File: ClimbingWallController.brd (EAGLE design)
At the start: 100 x 80 mm, 336 parts, among them IC1 74HCT138D, IC2 74HCT138D, IC3 PIC24FJ32GB004, IC4 SN74LV4052AD, IC5 SN74LV4052AD, IC6 TC1015, IC7 NCP1117, J1 PWR, Q1 NC, Q10 DPBT8105, Q11 DPBT8105, Q12 DPBT8105, Q13 DPBT8105, Q14 DPBT8105, Q15 DPBT8105, Q16 DPBT8105, Q18 DPBT8105, Q2 DPBT8105, Q3 DPBT8105, Q4 DPBT8105, Q5 DPBT8105, Q6 DPBT8105, Q7 DPBT8105, Q8 DPBT8105, Q9 DPBT8105, X1 MINI-USB-32005-201

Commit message: Iterated through a few possible board floorplans.  Routing will be incredibly tight, but I thought of a few possibilities that ease those concerns.
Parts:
- removed Q18: DPBT8105, Parts:SOT23
- removed ROW0: (no value), Parts:OSTVN08
- removed SG1: NC, buzzer:F/CM04P
- added JP2: BUZZER, pinhead:1X02
- added Q17: NC, transistor:SOT23-EBC
- added ROW2: (no value), Parts:OSTVN08
- C1, C9: value 10uF -> 22n; device rcl:C1206K -> resistor:C0603
- C10, C15: value 1uF -> 22n; device rcl:C0805 -> resistor:C0603
- C11, C12, C13, C14, C3, C4, C5: value 0.1uF -> 22n; device rcl:C0805 -> resistor:C0603
- C16: value 0.1uF -> NC; device rcl:C0805 -> rcl:C0603K
- C17, C29: value 1uF -> 0.1uF; device rcl:C0805 -> rcl:C0603K
- C18, C39, C89, C90, C91, C92, C93, C94, C95, C96, C97, C98: device rcl:C0805 -> rcl:C0603K
- C19: value 100uF -> 0.1uF; device resistor:PANASONIC_D -> rcl:C0603K
- C2, C6, C7: value NC -> 22n; device rcl:C0805 -> resistor:C0603
- C20: device resistor:C0805 -> resistor:C0603
- C21: value 100uF -> NC; device resistor:PANASONIC_D -> rcl:C0603K
- C22: value 22n -> NC; device resistor:C0805 -> rcl:C0603K
- C23: value 22n -> 470pF; device resistor:C0805 -> rcl:C0805
- C24, C38: value 22n -> 10uF; device resistor:C0805 -> rcl:C1206K
- C25: value 22n -> 1uF; device resistor:C0805 -> rcl:C0805
- C26, C27, C28, C31, C33: value 22n -> 0.1uF; device resistor:C0805 -> rcl:C0603K
- C30: value 100uF -> 1uF; device resistor:PANASONIC_D -> rcl:C0603K
- C32, C36: value 22n -> 1uF; device resistor:C0805 -> rcl:C0603K
- C34, C35, C37: value 22n -> 100uF; device resistor:C0805 -> resistor:PANASONIC_D
- C41, C42, C43, C44, C45, C46, C47, C48, C49, C50, C51, C52, C53, C54, C55, C56, C57, C58, C59, C60, C61, C62, C63, C64, C65, C66, C67, C68, C69, C70, C71, C72, C73, C74, C75, C76, C77, C78, C79, C80, C81, C82, C83, C84, C85, C86, C87, C88: device resistor:C0805 -> resistor:C0603K
- C8: value 470pF -> 22n; device rcl:C0805 -> resistor:C0603
- Q1: value NC -> DPBT8105; device transistor:SOT23-EBC -> Parts:SOT23
- R1, R10, R4: value 4.7k -> 20; device resistor:R0805 -> resistor:R0603
- R100, R101, R102, R103, R104, R105, R106, R107, R108, R109, R110, R111, R112, R113, R114, R115, R116, R117, R118, R119, R120, R121, R122, R123, R124, R125, R126, R127, R128, R129, R130, R131, R132, R133, R134, R135, R39, R40, R41, R42, R43, R44, R45, R46, R47, R48, R87, R88, R89, R90, R91, R92, R93, R94, R95, R96, R97, R98, R99: device resistor:R0805 -> resistor:R0603
- R11, R2, R5: value 4.7k -> 750; device resistor:R0805 -> resistor:R0603
- R12, R3, R6, R9: value 4.7k -> NC; device resistor:R0805 -> resistor:R0603
- R13, R16, R19, R22, R25, R28, R31, R34: value 390 -> 20; device resistor:R0805 -> resistor:R0603
- R14, R17, R20, R23, R26, R29, R32, R35: value 390 -> 750; device resistor:R0805 -> resistor:R0603
- R15, R18, R21, R24, R27, R30, R33: value 390 -> NC; device resistor:R0805 -> resistor:R0603
- R36: value 0 -> NC; device resistor:R0805 -> resistor:R0603
- R37: value NC -> 20; device resistor:R0805 -> resistor:R0603
- R38: value NC -> 750; device resistor:R0805 -> resistor:R0603
- R49, R52, R58: value 20 -> 4.7k; device resistor:R0805 -> resistor:R0603
- R50, R53, R59: value 750 -> 4.7k; device resistor:R0805 -> resistor:R0603
- R51, R54, R57, R60: value NC -> 4.7k; device resistor:R0805 -> resistor:R0603
- R55: value 20 -> 1.37k 0.5%
- R56: value 750 -> 1.37k 0.5%
- R61, R64, R67, R70, R73, R76, R79, R82: value 20 -> 390; device resistor:R0805 -> resistor:R0603
- R62, R65, R68, R71, R74, R77, R80, R83: value 750 -> 390; device resistor:R0805 -> resistor:R0603
- R63, R66, R69, R72, R75, R78, R81: value NC -> 390; device resistor:R0805 -> resistor:R0603
- R7: value 1.37k 0.5% -> 20; device resistor:R0805 -> resistor:R0603
- R8: value 1.37k 0.5% -> 750; device resistor:R0805 -> resistor:R0603
- R84: value NC -> 0
- R85: value 20 -> NC; device resistor:R0805 -> resistor:R0603
- R86: value 750 -> NC; device resistor:R0805 -> resistor:R0603
- moved C90 277.2 mm to (92.7, -58.4)
- moved C24 273.5 mm to (44.5, -102.9)
- moved C23 271.1 mm to (96.5, -49.5)
- moved C89 268.3 mm to (87.6, -58.4)
- moved D20 265.0 mm to (91.4, 26.7)
- moved C17 264.1 mm to (102.9, -49.5)
- moved C39 259.4 mm to (82.5, -58.4)
- moved C25 257.6 mm to (62.2, -58.4)
- moved D30 257.5 mm to (91.4, 52.1)
- moved C1 255.2 mm to (76.5, 11.7), turned to 270 degrees
- moved D19 253.4 mm to (91.4, 24.1)
- moved D40 251.4 mm to (91.4, 77.5)
- moved C18 250.7 mm to (109.2, -49.5)
- moved C61 246.6 mm to (88.6, 69.8)
- moved D29 245.3 mm to (91.4, 49.5)
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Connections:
- removed net N$31: Q1.B, R39.2
- removed net N$32: Q1.C, SG1.-
- removed net N$35: Q3.1, R44.2, R45.2
- removed net N$36: C22.1, R43.1
- removed net N$37: Q4.1, R47.2, R48.2
- removed net N$38: C23.1, R46.1
- removed net N$39: Q5.1, R50.2, R51.2
- removed net N$40: C24.1, R49.1
- removed net N$49: Q18.1, R65.2, R66.2
- removed net N$50: C31.1, R64.1
- removed net N$51: Q10.1, R68.2, R69.2
- removed net N$52: C32.1, R67.1
- removed net N$53: Q11.1, R71.2, R72.2
- removed net N$54: C33.1, R70.1
- removed net N$55: Q12.1, R74.2, R75.2
- removed net N$56: C34.1, R73.1
- removed net N$57: Q13.1, R77.2, R78.2
- removed net N$58: C35.1, R76.1
- removed net N$59: Q14.1, R80.2, R81.2
- removed net N$60: C36.1, R79.1
- removed net N$61: Q15.1, R83.2, R84.2
- removed net N$62: C37.1, R82.1
- removed net N$63: Q16.1, R86.2, R87.2
- removed net N$64: C38.1, R85.1
- new net N$65: R64.2, TCH0.3
- new net N$66: R65.2, TCH0.4
- new net N$67: R66.2, TCH0.5
- new net N$68: R67.2, TCH0.6
- new net N$69: R68.2, TCH0.7
- new net N$70: R69.2, TCH0.8
- new net N$71: R70.2, TCH0.9
- new net N$72: R71.2, TCH0.10
- new net N$73: R72.2, TCH0.11
- new net N$74: R74.2, TCH1.2
- new net N$75: R76.2, TCH1.4
- new net N$76: R78.2, TCH1.6
- new net N$77: R80.2, TCH1.8
- new net N$78: R82.2, TCH1.10
- new net N$79: R73.2, TCH1.1
- new net N$80: R75.2, TCH1.3
- new net N$81: R77.2, TCH1.5
- new net N$82: R79.2, TCH1.7
- new net N$83: R81.2, TCH1.9
- new net N$84: R83.2, TCH1.11
- new net N$85: C23.1, IC6.4
- new net N$86: R85.1, R86.2
- new net N$87: Q17.B, R87.2
- new net N$88: JP2.2, Q17.C
- net +3V3: now also C19.1, C24.1, C26.1, C27.1, C30.1, C31.1, C32.1, C33.1, R60.2, R85.2; no longer C11.1, C12.1, C15.1, C16.1, C3.1, C4.1, C5.1, C9.1, R12.2, R37.2
- net +5V: now also C25.1, C28.1, C34.+, C36.1, C37.+, JP2.1, Q1.2, R12.1, R15.1, R18.1, R21.1, R24.1, R27.1, R3.1, R30.1, R33.1, R36.1, R39.1, R6.1, R84.2, R9.1; no longer C10.1, C13.1, C14.1, C21.+, C30.+, Q18.2, R36.2, R51.1, R54.1, R57.1, R60.1, R63.1, R66.1, R69.1, R72.1, R75.1, R78.1, R81.1, R84.1, R87.1, SG1.+
- net CAIREF: now also R55.2; no longer R7.2
- net CAIREF1: now also R56.2; no longer R8.2
- net DISVREG: now also R59.2; no longer R11.2
- net GND: now also C19.2, C21.2, C30.2, C34.-, C35.-, C37.-, Q17.E, R49.1, R50.1, R51.1, R52.1, R53.1, R54.1, R55.1, R56.1, R57.1, R59.1, R86.1; no longer C19.-, C21.-, C30.-, C34.2, C35.2, C37.2, Q1.E, R1.1, R11.1, R2.1, R3.1, R38.1, R4.1, R5.1, R6.1, R7.1, R8.1, R9.1
- net MCLR_: now also R61.1; no longer R13.1
- net N$1: now also Q1.1, R2.2, R3.2; no longer C2.1, R12.1, R13.2
- net N$10: now also C5.1, R13.1; no longer R17.2, TCH0.4
- net N$11: now also Q7.1, R17.2; no longer TCH0.5
- net N$12: now also C6.1, R16.1; no longer R19.2, TCH0.6
- net N$13: now also Q8.1, R21.2; no longer TCH0.7
- net N$14: now also C7.1, R19.1; no longer R21.2, TCH0.8
- net N$15: now also Q9.1, R23.2, R24.2; no longer R22.2, TCH0.9
- net N$16: now also C8.1, R22.1; no longer R23.2, TCH0.10
- net N$17: now also Q10.1, R26.2, R27.2; no longer R24.2, TCH0.11
- net N$18: now also C9.1, R25.1; no longer R26.2, TCH1.2
- net N$19: now also Q11.1, R29.2, R30.2; no longer R28.2, TCH1.4
- net N$2: now also C1.1, R1.1; no longer IC1.4, IC1.5, R2.2
- net N$20: now also C10.1, R28.1; no longer R30.2, TCH1.6
- net N$21: now also Q12.1, R33.2; no longer TCH1.8
- net N$22: now also C11.1, R31.1; no longer R34.2, TCH1.10
- net N$23: now also Q13.1, R35.2, R36.2; no longer R25.2, TCH1.1
- net N$24: now also C12.1, R34.1; no longer R27.2, TCH1.3
- net N$25: now also Q14.1, R38.2, R39.2; no longer R29.2, TCH1.5
- net N$26: now also C13.1, R37.1; no longer R31.2, TCH1.7
- net N$27: now also Q15.1, R44.2, R45.2; no longer R33.2, TCH1.9
- net N$28: now also C14.1, R43.1; no longer R35.2, TCH1.11
- net N$29: now also Q16.1, R47.2, R48.2; no longer C8.1, IC6.4
- net N$3: now also Q3.1, R5.2, R6.2; no longer IC4.6, R3.2
- net N$30: now also C15.1, R46.1; no longer R37.1, R38.2
- net N$4: now also C2.1, R4.1; no longer IC3.42, R10.2
- net N$41: now also IC1.4, IC1.5, R50.2; no longer Q6.1, R53.2, R54.2
- net N$42: now also IC4.6, R51.2; no longer C25.1, R52.1
- net N$43: now also IC2.4, IC2.5, R53.2; no longer Q7.1, R56.2, R57.2
- net N$44: now also IC5.6, R54.2; no longer C26.1, R55.1
- net N$45: now also IC3.42, R58.2; no longer Q8.1, R59.2, R60.2
- net N$46: now also C16.1, R60.1, R61.2; no longer C27.1, R58.1
- net N$47: now also TCH0.1; no longer Q9.1, R63.2
- net N$48: now also R63.2, TCH0.2; no longer C28.1, R61.1
- net N$5: now also Q4.1, R8.2, R9.2; no longer IC2.4, IC2.5, R5.2
- net N$6: now also C3.1, R7.1; no longer IC5.6, R6.2
- net N$7: now also Q5.1, R11.2, R12.2; no longer R14.2, TCH0.1
- net N$8: now also C4.1, R10.1; no longer R15.2, TCH0.2
- net N$9: now also Q6.1, R14.2, R15.2; no longer R16.2, TCH0.3
- net OSCI: now also C22.1; no longer C7.1
- net OSCO: now also C21.1; no longer C6.1
- net RAEN: now also R49.2; no longer R1.2
- net RBEN: now also R52.2; no longer R4.2
- net ROW0: now also Q1.3, R1.2, ROW1.1; no longer Q2.3, R40.2, ROW0.1
- net ROW0EN_: now also R2.1; no longer R41.1
- net ROW1: now also Q2.3, R40.2, ROW1.2; no longer Q3.3, R43.2, ROW0.2
- net ROW10: now also D12.C, Q12.3, R31.2, ROW2.4; no longer D11.C, Q11.3, R70.2, ROW1.3
- net ROW10EN_: now also R32.1; no longer R71.1
- net ROW11: now also D14.C, Q14.3, R37.2, ROW2.5; no longer D12.C, Q12.3, R73.2, ROW1.4
- net ROW11EN_: now also R38.1; no longer R74.1
- net ROW12: now also D15.C, Q15.3, R43.2, ROW2.7; no longer D13.C, Q13.3, R76.2, ROW1.5
- net ROW12EN_: now also R44.1; no longer R77.1
- net ROW13: now also D16.C, Q16.3, R46.2, ROW2.8; no longer D14.C, Q14.3, R79.2, ROW1.6
- net ROW13EN_: now also R47.1; no longer R80.1
- net ROW14: now also D9.C, Q9.3, R22.2, ROW2.2; no longer D15.C, Q15.3, R82.2, ROW1.7
- net ROW14EN_: now also R23.1; no longer R83.1
- net ROW15: now also D13.C, Q13.3, R34.2, ROW2.6; no longer D16.C, Q16.3, R85.2, ROW1.8
- net ROW15EN_: now also R35.1; no longer R86.1
- net ROW1EN_: now also R41.1; no longer R44.1
- net ROW2: now also Q3.3, R4.2, ROW1.3; no longer Q4.3, R46.2, ROW0.3
- net ROW2EN_: now also R5.1; no longer R47.1
- net ROW3: now also Q4.3, R7.2, ROW1.4; no longer Q5.3, R49.2, ROW0.4
- net ROW3EN_: now also R8.1; no longer R50.1
- net ROW4: now also D6.C, R13.2, ROW1.5; no longer D5.C, R52.2, ROW0.5
- net ROW4EN_: now also R14.1; no longer R53.1
- net ROW5: now also D5.C, Q5.3, R10.2, ROW1.6; no longer D6.C, Q7.3, R55.2, ROW0.6
- net ROW5EN_: now also R11.1; no longer R56.1
- net ROW6: now also Q7.3, R16.2, ROW1.7; no longer Q8.3, R58.2, ROW0.7
- net ROW6EN_: now also R17.1; no longer R59.1
- net ROW7: now also Q8.3, R19.2, ROW1.8; no longer Q9.3, R61.2, ROW0.8
- net ROW7EN_: now also R20.1; no longer R62.1
- net ROW8: now also D10.C, Q10.3, R25.2, ROW2.1; no longer D9.C, Q18.3, R64.2, ROW1.1
- net ROW8EN_: now also R26.1; no longer R65.1
- net ROW9: now also D11.C, Q11.3, R28.2, ROW2.3; no longer D10.C, Q10.3, R67.2, ROW1.2
- net ROW9EN_: now also R29.1; no longer R68.1
- net TOUCH0: now also R62.1; no longer R14.1
- net TOUCH1: now also R63.1; no longer R15.1
- net TOUCH10: now also R72.1; no longer R24.1
- net TOUCH11: now also R73.1; no longer R25.1
- net TOUCH12: now also R74.1; no longer R26.1
- net TOUCH13: now also R75.1; no longer R27.1
- net TOUCH14: now also R76.1; no longer R28.1
- net TOUCH15: now also R77.1; no longer R29.1
- net TOUCH16: now also R78.1; no longer R30.1
- net TOUCH17: now also R79.1; no longer R31.1
- net TOUCH18: now also R80.1; no longer R32.1
- net TOUCH19: now also R81.1; no longer R33.1
- net TOUCH2: now also R64.1; no longer R16.1
- net TOUCH20: now also R82.1; no longer R34.1
- net TOUCH21: now also R83.1; no longer R35.1
- net TOUCH3: now also R65.1; no longer R17.1
- net TOUCH4: now also R66.1; no longer R18.1
- net TOUCH5: now also R67.1; no longer R19.1
- net TOUCH6: now also R68.1; no longer R20.1
- net TOUCH7: now also R69.1; no longer R21.1
- net TOUCH8: now also R70.1; no longer R22.1
- net TOUCH9: now also R71.1; no longer R23.1
- net V+: now also C35.+, R84.1; no longer C19.+, R36.1
- net VBUS: now also R57.2, R58.1; no longer R10.1, R9.2
- net VDDCORE: now also C38.1; no longer C1.1
- net VREF+: now also R87.1; no longer R39.1
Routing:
- net +5V: track 0.00 -> 98.2 mm
- net GND: track 0.00 -> 42.5 mm
- net ROW13: track 0.00 -> 18.6 mm
- net ROW7: track 0.00 -> 18.6 mm
- net ROW10: track 0.00 -> 17.6 mm
- net ROW3: track 0.00 -> 17.6 mm
- net ROW1: track 0.00 -> 17.6 mm
- net ROW14: track 0.00 -> 17.6 mm
- net ROW2: track 0.00 -> 14.8 mm
- net ROW0: track 0.00 -> 14.8 mm
- net ROW9: track 0.00 -> 14.8 mm
- net ROW8: track 0.00 -> 14.8 mm
- net ROW15: track 0.00 -> 13.4 mm
- net ROW5: track 0.00 -> 13.4 mm
- net ROW4: track 0.00 -> 10.6 mm
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
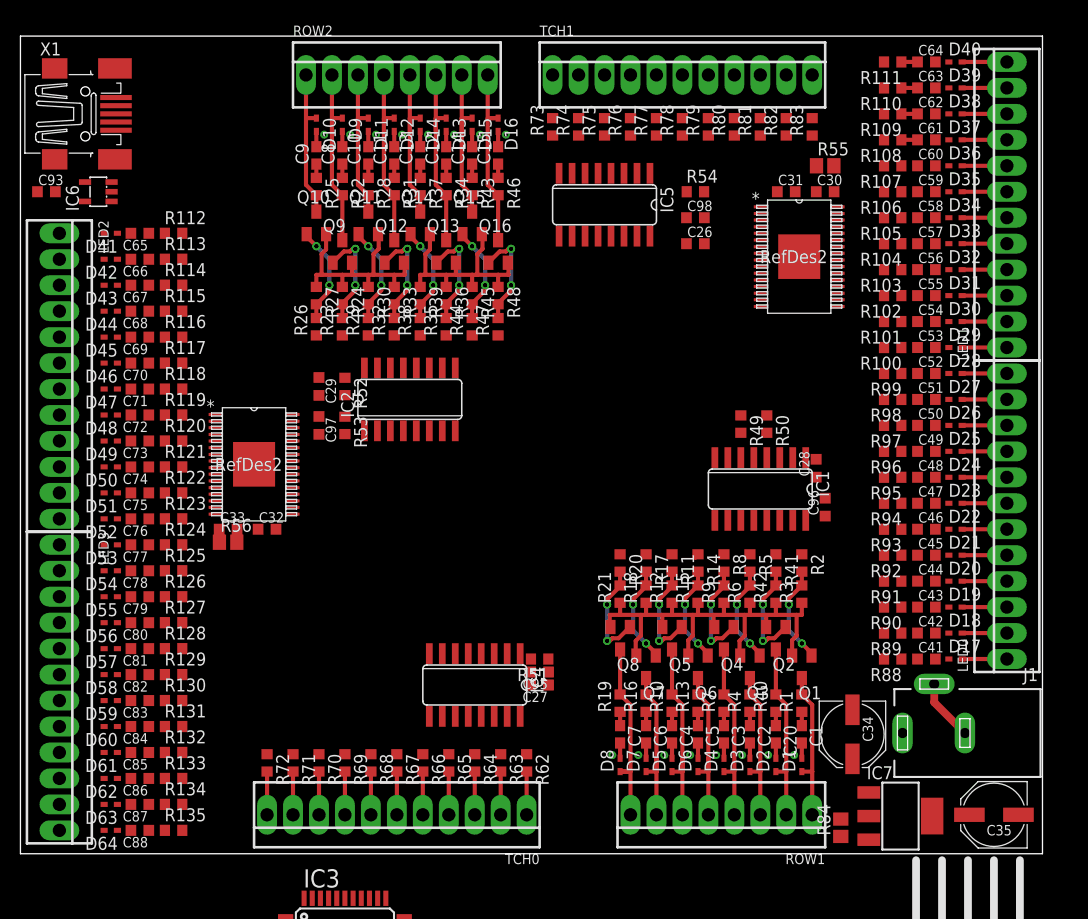
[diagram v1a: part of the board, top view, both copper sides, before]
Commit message: Completed most of the column driver routing.
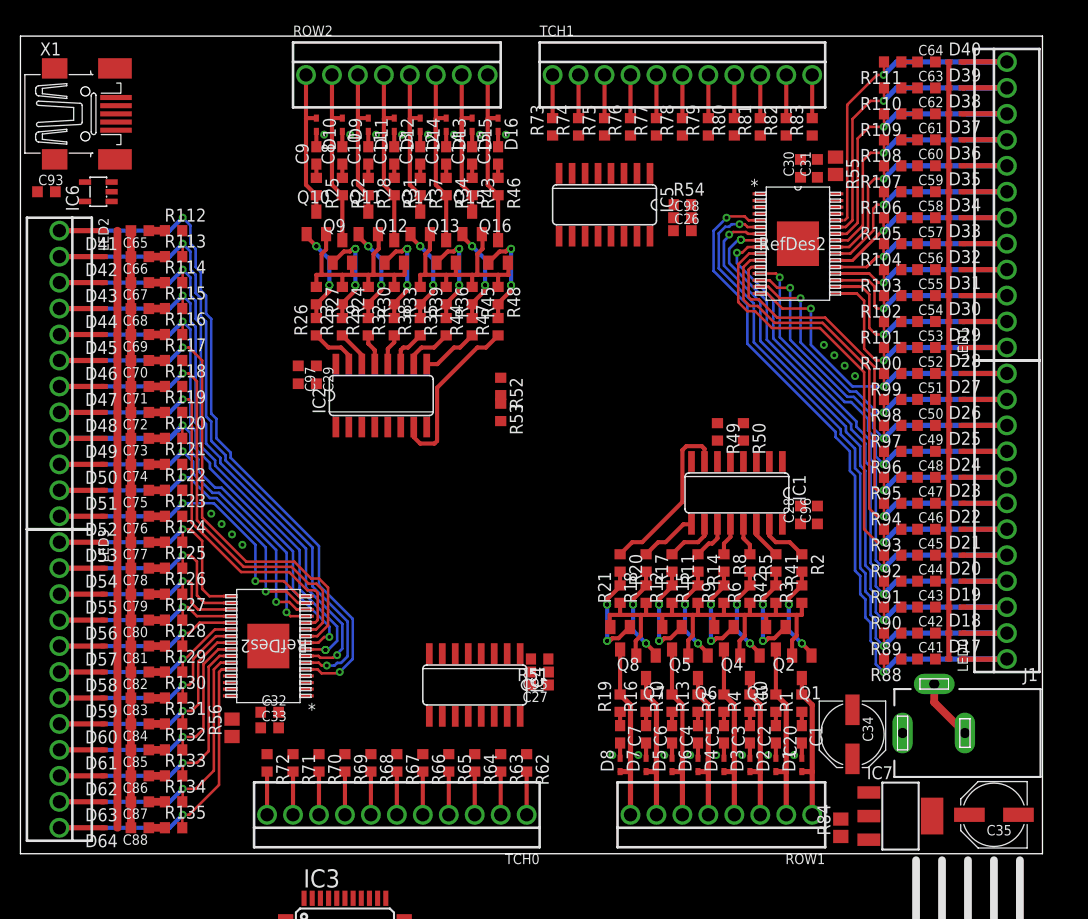
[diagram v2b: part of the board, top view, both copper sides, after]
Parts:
- moved C33 19.9 mm to (24.4, 12.3)
- moved R56 18.2 mm to (20.7, 12.3), turned to 90 degrees
- moved C32 17.9 mm to (24.4, 13.8)
- moved U$2 17.8 mm to (24.3, 20.3), turned to 180 degrees
- moved R53 15.3 mm to (47.0, 43.2)
- moved R52 15.2 mm to (47.0, 45.7)
- moved C97 5.35 mm to (27.2, 46.9)
- moved C28 4.82 mm to (76.3, 33.1)
- moved C31 3.81 mm to (78.0, 67.1), turned to 90 degrees
- moved C30 3.32 mm to (76.3, 67.1), turned to 90 degrees
- moved IC2 2.82 mm to (35.3, 44.8)
- moved R49 2.41 mm to (68.2, 41.3)
- moved R50 2.41 mm to (70.7, 41.3)
- moved IC1 2.32 mm to (70.1, 35.3)
- moved C26 1.80 mm to (64.8, 61.0)
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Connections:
- net ROW10: now also D11.C, Q11.3, R28.2, ROW2.3; no longer D12.C, Q12.3, R31.2, ROW2.4
- net ROW10EN_: now also R29.1; no longer R32.1
- net ROW11: now also D12.C, Q12.3, R31.2, ROW2.4; no longer D14.C, Q14.3, R37.2, ROW2.5
- net ROW11EN_: now also R32.1; no longer R38.1
- net ROW12: now also D14.C, Q14.3, R37.2, ROW2.5; no longer D15.C, Q15.3, R43.2, ROW2.7
- net ROW12EN_: now also R38.1; no longer R44.1
- net ROW13: now also D13.C, Q13.3, R34.2, ROW2.6; no longer D16.C, Q16.3, R46.2, ROW2.8
- net ROW13EN_: now also R35.1; no longer R47.1
- net ROW14: now also D15.C, Q15.3, R43.2, ROW2.7; no longer D9.C, Q9.3, R22.2, ROW2.2
- net ROW14EN_: now also R44.1; no longer R23.1
- net ROW15: now also D16.C, Q16.3, R46.2, ROW2.8; no longer D13.C, Q13.3, R34.2, ROW2.6
- net ROW15EN_: now also R47.1; no longer R35.1
- net ROW9: now also D9.C, Q9.3, R22.2, ROW2.2; no longer D11.C, Q11.3, R28.2, ROW2.3
- net ROW9EN_: now also R23.1; no longer R29.1
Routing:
- net +5V: track 98.2 -> 215.1 mm
- net R8: track 0.00 -> 72.2 mm, vias 0 -> 2
- net G8: track 0.00 -> 69.7 mm, vias 0 -> 2
- net R0: track 4.38 -> 73.5 mm, vias 0 -> 2
- net B8: track 0.00 -> 65.7 mm, vias 0 -> 2
- net G0: track 4.38 -> 69.7 mm, vias 0 -> 2
- net R9: track 0.00 -> 61.6 mm, vias 0 -> 2
- net B0: track 4.38 -> 65.8 mm, vias 0 -> 2
- net GND: track 42.5 -> 100.9 mm
- net G9: track 0.00 -> 57.4 mm, vias 0 -> 2
- net R1: track 4.38 -> 61.6 mm, vias 0 -> 2
- net B9: track 0.00 -> 56.1 mm, vias 0 -> 1
- net G1: track 4.38 -> 57.5 mm, vias 0 -> 2
- net B1: track 4.38 -> 57.4 mm, vias 0 -> 1
- net R10: track 0.00 -> 52.4 mm, vias 0 -> 1
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
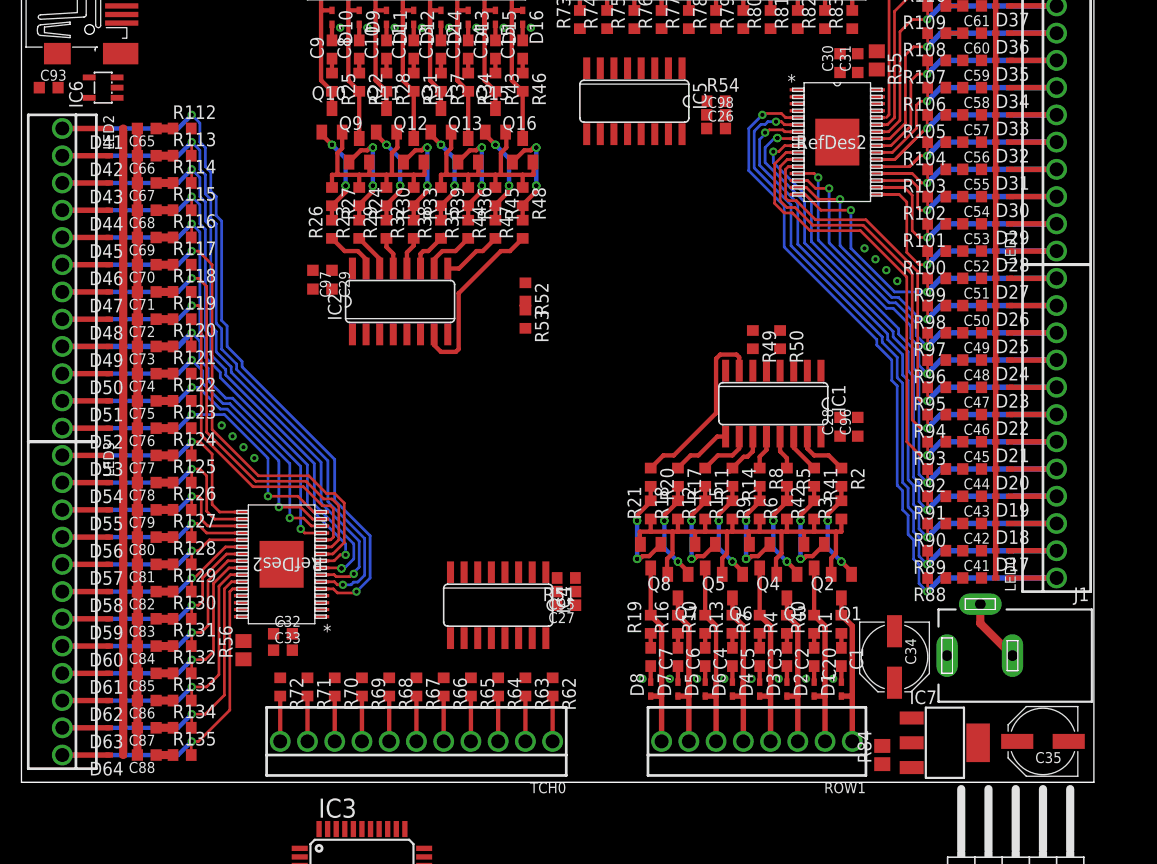
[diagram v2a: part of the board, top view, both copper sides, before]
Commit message: Completed row/column routing.
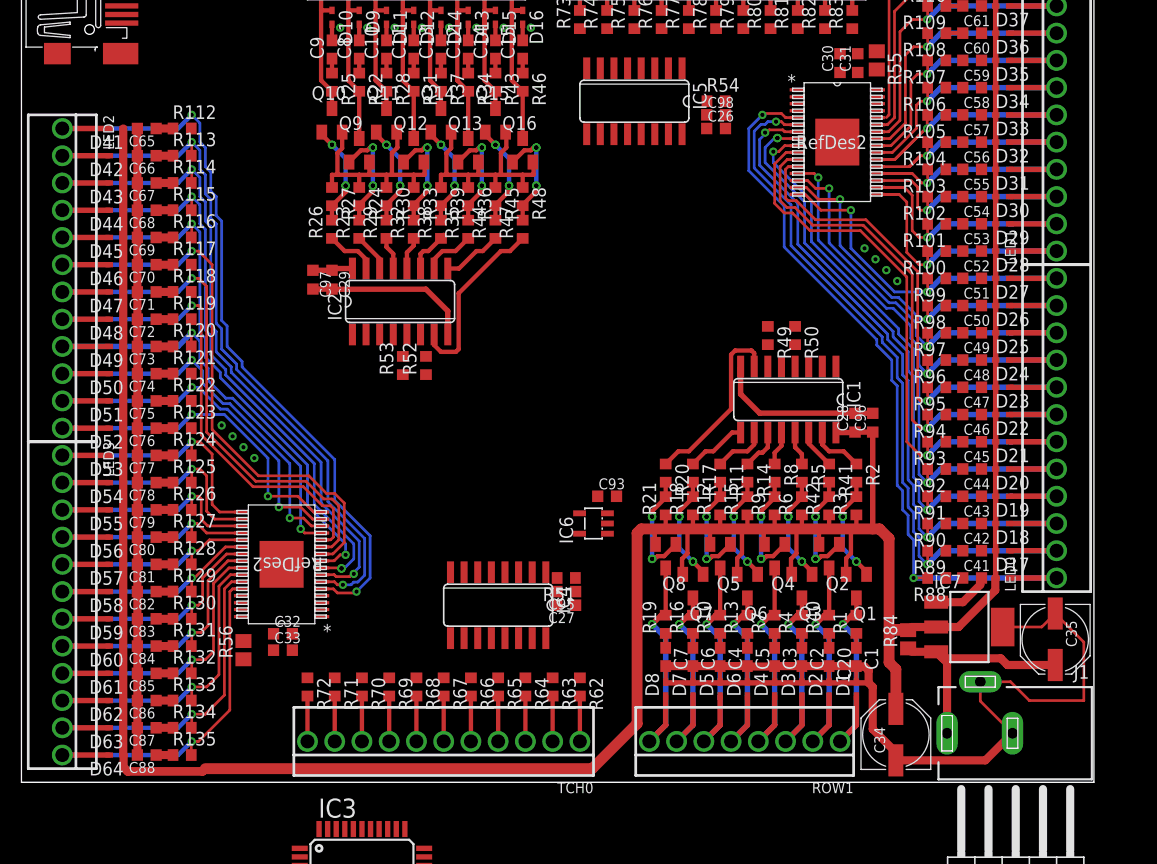
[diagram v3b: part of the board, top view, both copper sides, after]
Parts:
- moved C93 64.5 mm to (54.6, 26.7)
- moved IC6 61.2 mm to (53.3, 24.1)
- moved R53 12.2 mm to (35.6, 38.9), turned to 90 degrees
- moved R52 11.5 mm to (37.7, 38.9), turned to 90 degrees
- moved R84 11.1 mm to (82.7, 13.3)
- moved IC7 11.0 mm to (88.4, 14.5)
- moved C35 9.59 mm to (96.4, 13.3), turned to 270 degrees
- moved C34 7.24 mm to (81.5, 4.45), turned to 90 degrees
- moved J1 7.24 mm to (89.4, 4.57)
- moved R65 2.54 mm to (44.5, 8.89)
- moved R72 2.54 mm to (26.7, 8.89)
- moved R62 2.54 mm to (52.1, 8.89)
- moved R63 2.54 mm to (49.5, 8.89)
- moved R64 2.54 mm to (47.0, 8.89)
- moved R66 2.54 mm to (41.9, 8.89)
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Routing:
- net +5V: track 215.1 -> 338.9 mm
- net GND: track 100.9 -> 216.5 mm
- net V+: track 0.00 -> 22.4 mm
- net ROW4: track 10.6 -> 20.5 mm, vias 0 -> 1
- net ROW5: track 13.4 -> 23.3 mm, vias 0 -> 1
- net ROW6: track 10.6 -> 20.5 mm, vias 0 -> 1
- net ROW1: track 17.6 -> 23.3 mm, vias 0 -> 1
- net ROW2: track 14.8 -> 20.5 mm, vias 0 -> 1
- net ROW0: track 14.8 -> 20.5 mm, vias 0 -> 1
- net ROW3: track 17.6 -> 23.3 mm, vias 0 -> 1
- net S$2: track 5.53 -> 0.00 mm
- net S$1: track 5.53 -> 0.00 mm
- net ROW7: track 18.6 -> 23.3 mm, vias 0 -> 1
- net R0: track 73.5 -> 72.5 mm

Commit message: Made progress on layout.
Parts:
- C23, C25: device rcl:C0805 -> rcl:C0603K
- moved C24 130.8 mm to (54.4, 27.6)
- moved C23 84.5 mm to (56.0, 24.6), turned to 270 degrees
- moved C25 79.5 mm to (55.0, 20.7)
- moved C37 71.6 mm to (54.4, 15.5), turned to 90 degrees
- moved IC3 55.9 mm to (52.1, 41.9)
- moved C93 22.9 mm to (67.3, 45.7)
- moved C95 14.2 mm to (38.0, 11.7), turned to 0 degrees
- moved C27 12.3 mm to (40.9, 23.7), turned to 0 degrees
- moved R54 11.3 mm to (54.4, 59.2), turned to 90 degrees
- moved C26 7.91 mm to (58.9, 55.6)
- moved C98 6.65 mm to (61.8, 68.2)
- moved R51 5.06 mm to (46.0, 20.6), turned to 270 degrees
- moved IC4 4.02 mm to (40.6, 17.8), turned to 90 degrees
- moved IC5 2.96 mm to (59.7, 62.0), turned to 270 degrees
- moved C10 2.54 mm to (31.5, 68.3)
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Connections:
- net TOUCH0: now also IC3.23; no longer IC4.1
- net TOUCH1: now also IC3.20; no longer IC4.5
- net TOUCH10: now also IC4.11; no longer IC3.23
- net TOUCH2: now also IC3.15; no longer IC4.2
- net TOUCH3: now also IC4.2; no longer IC4.4
- net TOUCH4: now also IC4.1; no longer IC4.12
- net TOUCH5: now also IC4.4; no longer IC4.14
- net TOUCH6: now also IC4.5; no longer IC4.15
- net TOUCH7: now also IC4.15; no longer IC4.11
- net TOUCH8: now also IC4.14; no longer IC3.15
- net TOUCH9: now also IC4.12; no longer IC3.20
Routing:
- net GND: track 216.5 -> 236.1 mm
- net TOUCH0: track 0.00 -> 15.5 mm
- net TOUCH1: track 0.00 -> 14.8 mm
- net TOUCH2: track 0.00 -> 14.8 mm
- net +3V3: track 0.00 -> 14.5 mm
- net TOUCH6: track 0.00 -> 13.2 mm
- net TMUX0: track 0.00 -> 10.1 mm
- net TOUCH5: track 0.00 -> 10.1 mm
- net TMUX1: track 0.00 -> 8.04 mm
- net TOUCH3: track 0.00 -> 6.13 mm
- net TOUCH4: track 0.00 -> 4.34 mm
- net N$42: track 0.00 -> 2.28 mm
